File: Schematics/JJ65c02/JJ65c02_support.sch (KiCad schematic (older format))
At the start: 26 parts, among them SW1 RESET, U1 NE555, U2 74HC00, U3 74AC138, U4 74HC08, U5 MAX232B, U6 LM386, X1 1Mhz, X2 1.8Mhz

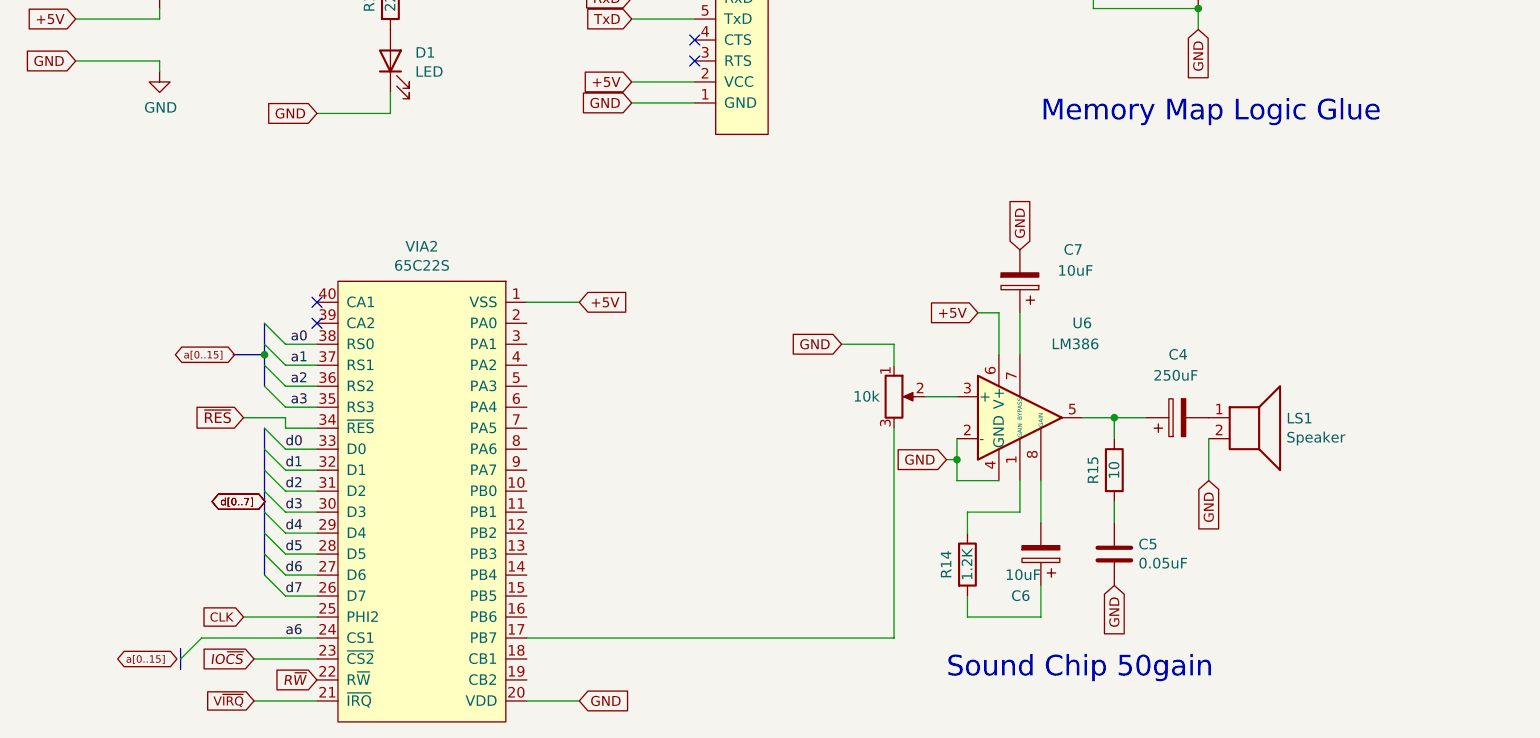
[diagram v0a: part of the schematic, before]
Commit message: Add in basic sound capability
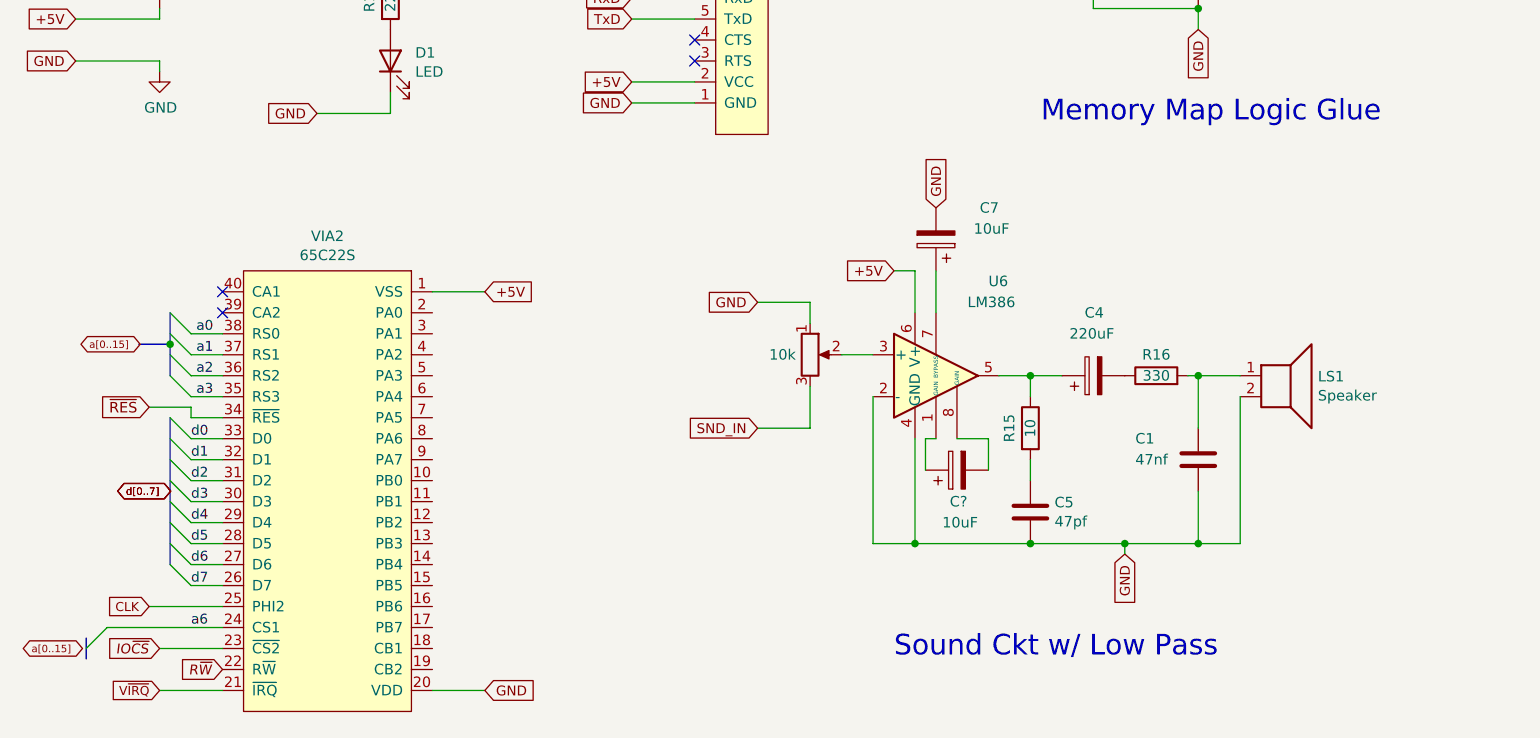
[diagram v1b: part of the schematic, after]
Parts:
- removed C6: 10uF, Capacitor_THT:C_Disc_D3.4mm_W2.1mm_P2.50mm, symbol Device:CP
- removed R14: 1.2K, Resistor_THT:R_Axial_DIN0207_L6.3mm_D2.5mm_P7.62mm_Horizontal, symbol Device:R
- added C1: 47nf, Capacitor_THT:C_Disc_D3.4mm_W2.1mm_P2.50mm, symbol Device:C
- added C?: 10uF, Capacitor_THT:C_Disc_D3.4mm_W2.1mm_P2.50mm, symbol Device:CP
- added R16: 330, Resistor_THT:R_Axial_DIN0207_L6.3mm_D2.5mm_P7.62mm_Horizontal, symbol Device:R
- C4: value 250uF -> 220uF
- C5: value 0.05uF -> 47pf
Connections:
- net GND: now also C1.2
- net at VIA2.17 (PB7): no longer RV2.3
- net at U6.1 (GAIN): now also C?.1
- net at U6.8 (GAIN): now also C?.2
- net at C4.2: now also R16.1; no longer LS1.1
- new net: C1.1, LS1.1, R16.2
- new net SND_IN: RV2.3
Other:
- note added: "Sound Ckt w/ Low Pass"
- note removed: "Sound Chip 50gain"
- moved on the sheet: C4, C5, C7, LS1, R15, U6, VIA2

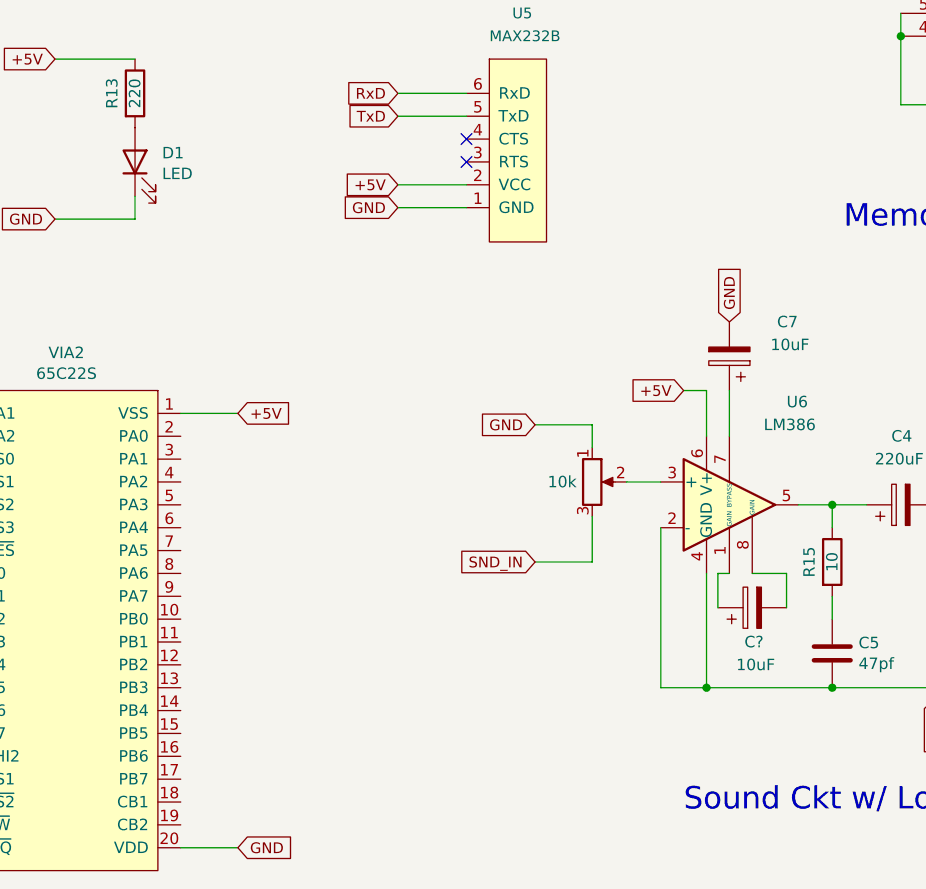
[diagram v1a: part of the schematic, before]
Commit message: Add the SND output to an LED indicator as well as the input to the amp
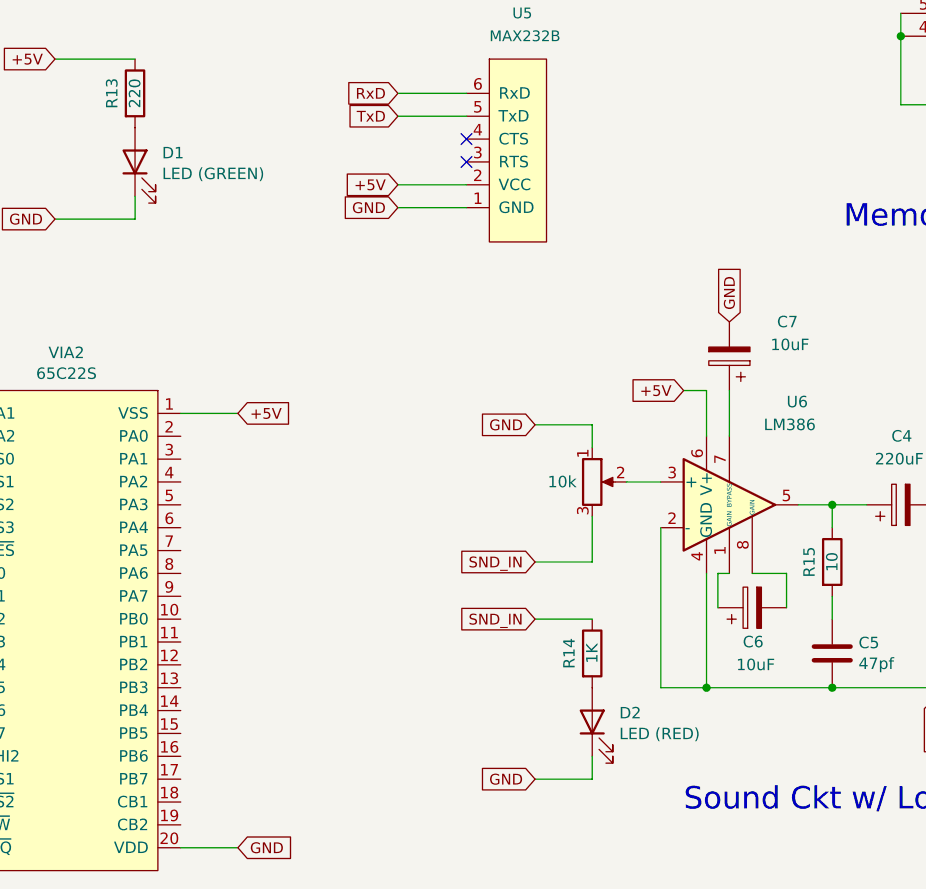
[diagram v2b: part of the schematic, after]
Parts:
- added D2: LED (RED), symbol Device:LED
- added R14: 1K, Resistor_THT:R_Axial_DIN0207_L6.3mm_D2.5mm_P7.62mm_Horizontal, symbol Device:R
- D1: value LED -> LED (GREEN)
- gave numbers to parts that had none: 1
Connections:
- net GND: now also D2.1 (K)
- net SND_IN: now also R14.1
- new net: D2.2 (A), R14.2
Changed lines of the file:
@@
 P 2450 3650
 F 0 "D1" V 2489 3532 50  0000 R CNN
-F 1 "LED" V 2398 3532 50  0000 R CNN
+F 1 "LED (GREEN)" V 2398 3532 50  0000 R CNN
 F 2 "" H 2450 3650 50  0001 C CNN
 F 3 "~" H 2450 3650 50  0001 C CNN
@@
 	4450 5400 4200 5400
 $Comp
-L Device:CP C?
+L Device:CP C6
 U 1 1 61A13E6D
 P 5150 5600
-AR Path="/61660CAC/61A13E6D" Ref="C?"  Part="1"
+AR Path="/61660CAC/61A13E6D" Ref="C6"  Part="1"
 AR Path="/61610474/61A13E6D" Ref="C?"  Part="1"
-F 0 "C?" V 5000 5550 50  0000 L CNN
+F 0 "C6" V 5000 5550 50  0000 L CNN
 F 1 "10uF" V 4900 5500 50  0000 L CNN
 F 2 "Capacitor_THT:C_Disc_D3.4mm_W2.1mm_P2.50mm" H 5188 5450 50  0001 C CNN
@@
 Wire Wire Line
 	5300 5450 5300 5600
+$Comp
+L Device:LED D2
+U 1 1 61AAFD1D
+P 4450 6100
+F 0 "D2" V 4489 5982 50  0000 R CNN
+F 1 "LED (RED)" V 4398 5982 50  0000 R CNN
+F 2 "" H 4450 6100 50  0001 C CNN
+F 3 "~" H 4450 6100 50  0001 C CNN
+	1    4450 6100
+	0    -1   -1   0
+$EndComp
+$Comp
+L Device:R R14
+U 1 1 61AAFD23
+P 4450 5800
+AR Path="/61660CAC/61AAFD23" Ref="R14"  Part="1"
+AR Path="/61610474/61AAFD23" Ref="R?"  Part="1"
+F 0 "R14" V 4350 5800 50  0000 C CNN
+F 1 "1K" V 4450 5800 50  0000 C CNN
+F 2 "Resistor_THT:R_Axial_DIN0207_L6.3mm_D2.5mm_P7.62mm_Horizontal" V 4380 5800 50  0001 C CNN
+F 3 "~" H 4450 5800 50  0001 C CNN
+	1    4450 5800
+	1    0    0    -1
+$EndComp
+Text GLabel 4200 5650 0    47   Input ~ 0
+SND_IN
+Text GLabel 4200 6350 0    47   Input ~ 0
+GND
+Wire Wire Line
+	4450 6350 4450 6250
+Wire Wire Line
+	4200 5650 4450 5650
+Wire Wire Line
+	4450 6350 4200 6350
 Wire Bus Line
 	1000 6400 1000 6500

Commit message: 2nd VIA
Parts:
- added A?: Arduino_Nano_v2.x, Module:Arduino_Nano, symbol MCU_Module:Arduino_Nano_v2.x
- added J?: Mini-DIN-6, symbol Connector:Mini-DIN-6
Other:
- moved on the sheet: X1, X2
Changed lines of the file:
@@
 L Oscillator:CXO_DIP14 X?
 U 1 1 6171CEB1
-P 8800 3650
+P 8700 3300
 AR Path="/6171CEB1" Ref="X?"  Part="1"
 AR Path="/61660CAC/6171CEB1" Ref="X1"  Part="1"
 AR Path="/61610474/6171CEB1" Ref="X?"  Part="1"
-F 0 "X1" H 8900 3900 50  0000 L CNN
-F 1 "1Mhz" H 8950 4000 50  0000 L CNN
-F 2 "Oscillator:Oscillator_DIP-14" H 9250 3300 50  0001 C CNN
-F 3 "http://cdn-reichelt.de/documents/datenblatt/B400/OSZI.pdf" H 8700 3650 50  0001 C CNN
-	1    8800 3650
-	1    0    0    -1
-$EndComp
-Text GLabel 9100 3650 2    43   Output ~ 0
+F 0 "X1" H 8800 3550 50  0000 L CNN
+F 1 "1Mhz" H 8850 3650 50  0000 L CNN
+F 2 "Oscillator:Oscillator_DIP-14" H 9150 2950 50  0001 C CNN
+F 3 "http://cdn-reichelt.de/documents/datenblatt/B400/OSZI.pdf" H 8600 3300 50  0001 C CNN
+	1    8700 3300
+	1    0    0    -1
+$EndComp
+Text GLabel 9000 3300 2    43   Output ~ 0
 CLK
 $Comp
 L power:+5V #PWR?
 U 1 1 6171CEBE
-P 8850 3700
+P 8750 3350
 AR Path="/6171CEBE" Ref="#PWR?"  Part="1"
 AR Path="/61660CAC/6171CEBE" Ref="#PWR020"  Part="1"
 AR Path="/61610474/6171CEBE" Ref="#PWR?"  Part="1"
-F 0 "#PWR020" H 8850 3550 50  0001 C CNN
-F 1 "+5V" H 8865 3873 50  0000 C CNN
-F 2 "" H 8850 3700 50  0001 C CNN
-F 3 "" H 8850 3700 50  0001 C CNN
-	1    8850 3700
-	1    0    0    -1
-$EndComp
-NoConn ~ 8500 3650
+F 0 "#PWR020" H 8750 3200 50  0001 C CNN
+F 1 "+5V" H 8765 3523 50  0000 C CNN
+F 2 "" H 8750 3350 50  0001 C CNN
+F 3 "" H 8750 3350 50  0001 C CNN
+	1    8750 3350
+	1    0    0    -1
+$EndComp
+NoConn ~ 8400 3300
 $Comp
 L Oscillator:CXO_DIP14 X?
 U 1 1 6171CEC5
-P 10150 3650
+P 10050 3300
 AR Path="/6171CEC5" Ref="X?"  Part="1"
 AR Path="/61660CAC/6171CEC5" Ref="X2"  Part="1"
 AR Path="/61610474/6171CEC5" Ref="X?"  Part="1"
-F 0 "X2" H 10250 3900 50  0000 L CNN
-F 1 "1.8Mhz" H 10300 4000 50  0000 L CNN
-F 2 "Oscillator:Oscillator_DIP-14" H 10600 3300 50  0001 C CNN
-F 3 "http://cdn-reichelt.de/documents/datenblatt/B400/OSZI.pdf" H 10050 3650 50  0001 C CNN
-	1    10150 3650
-	1    0    0    -1
-$EndComp
-Text GLabel 10450 3650 2    43   Output ~ 0
+F 0 "X2" H 10150 3550 50  0000 L CNN
+F 1 "1.8Mhz" H 10200 3650 50  0000 L CNN
+F 2 "Oscillator:Oscillator_DIP-14" H 10500 2950 50  0001 C CNN
+F 3 "http://cdn-reichelt.de/documents/datenblatt/B400/OSZI.pdf" H 9950 3300 50  0001 C CNN
+	1    10050 3300
+	1    0    0    -1
+$EndComp
+Text GLabel 10350 3300 2    43   Output ~ 0
 ACIA-CLK
-NoConn ~ 9850 3650
+NoConn ~ 9750 3300
 $Comp
 L 74xx:74HC00 U2
@@
 a12
 Wire Wire Line
-	8800 3300 8800 3350
+	8700 2950 8700 3000
 $Comp
 L 74xx:74LS138 U3
@@
 Text GLabel 1200 2400 0    47   Input ~ 0
 GND
-Text GLabel 10150 4000 3    47   Input ~ 0
+Text GLabel 10050 3650 3    47   Input ~ 0
 GND
 Text GLabel 6300 3500 3    47   Input ~ 0
@@
 Text GLabel 6700 2050 1    47   Input ~ 0
 +5V
-Text GLabel 8800 3300 1    47   Input ~ 0
-+5V
-Text GLabel 10150 3250 1    47   Input ~ 0
-+5V
-Text GLabel 8800 3950 3    47   Input ~ 0
-GND
-Wire Wire Line
-	10150 3250 10150 3350
-Wire Wire Line
-	10150 3950 10150 4000
+Text GLabel 8700 2950 1    47   Input ~ 0
++5V
+Text GLabel 10050 2900 1    47   Input ~ 0
++5V
+Text GLabel 8700 3600 3    47   Input ~ 0
+GND
+Wire Wire Line
+	10050 2900 10050 3000
+Wire Wire Line
+	10050 3600 10050 3650
 $Comp
 L 74xx:74LS08 U4
@@
 Wire Wire Line
 	4450 6350 4200 6350
+$Comp
+L MCU_Module:Arduino_Nano_v2.x A?
+U 1 1 61B02721
+P 7950 5150
+F 0 "A?" H 7950 4061 50  0000 C CNN
+F 1 "Arduino_Nano_v2.x" H 7950 3970 50  0000 C CNN
+F 2 "Module:Arduino_Nano" H 7950 5150 50  0001 C CIN
+F 3 "https://www.arduino.cc/en/uploads/Main/ArduinoNanoManual23.pdf" H 7950 5150 50  0001 C CNN
+	1    7950 5150
+	1    0    0    -1
+$EndComp
+$Comp
+L Connector:Mini-DIN-6 J?
+U 1 1 61B062BD
+P 9800 5200
+F 0 "J?" H 9800 5567 50  0000 C CNN
+F 1 "Mini-DIN-6" H 9800 5476 50  0000 C CNN
+F 2 "" H 9800 5200 50  0001 C CNN
+F 3 "http://service.powerdynamics.com/ec/Catalog17/Section%2011.pdf" H 9800 5200 50  0001 C CNN
+	1    9800 5200
+	1    0    0    -1
+$EndComp
 Wire Bus Line
 	1000 6400 1000 6500

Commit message: PCB work
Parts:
- removed D2: LED (RED), symbol Device:LED
- removed R14: 1K, Resistor_THT:R_Axial_DIN0207_L6.3mm_D2.5mm_P7.62mm_Horizontal, symbol Device:R
- removed R2: 4.7K, Resistor_THT:R_Axial_DIN0207_L6.3mm_D2.5mm_P7.62mm_Horizontal, symbol Device:R
- removed U4: 74HC08, Package_DIP:DIP-14_W7.62mm_Socket, symbol 74xx:74LS08
- added J2: Barrel_Jack, Connector_BarrelJack:CUI_PJ-059AH, symbol Connector:Barrel_Jack_Switch_Pin3Ring
- added J3: VIA2 PortB, Connector_PinSocket_2.54mm:PinSocket_1x10_P2.54mm_Vertical, symbol Connector_Generic:Conn_01x10
- added J4: Arduino Jack1, Connector_PinSocket_2.54mm:PinSocket_1x14_P2.54mm_Vertical, symbol Connector_Generic:Conn_01x14
- added J5: Arduino Jack2, Connector_PinSocket_2.54mm:PinSocket_1x14_P2.54mm_Vertical, symbol Connector_Generic:Conn_01x14
- added J6: AudioJack2, Connector_Audio:Jack_3.5mm_CUI_SJ1-3533NG_Horizontal, symbol Connector:AudioJack3
- added SW2: SW_SPST, Button_Switch_THT:SW_DIP_SPSTx01_Slide_6.7x4.1mm_W7.62mm_P2.54mm_LowProfile, symbol Switch:SW_SPST
- added unit 5 of U3
- added U7: LM2940T-5.0/LF08, Connector:LM2940, symbol Regulator_Linear:LM2936-5.0
- C3: renamed from C7; footprint Capacitor_THT:C_Disc_D3.4mm_W2.1mm_P2.50mm -> Capacitor_THT:CP_Radial_D5.0mm_P2.50mm
- C4: renamed from C6; footprint Capacitor_THT:C_Disc_D3.4mm_W2.1mm_P2.50mm -> Capacitor_THT:CP_Radial_D5.0mm_P2.50mm
- C6: renamed from C4; footprint Capacitor_THT:C_Disc_D3.4mm_W2.1mm_P2.50mm -> Capacitor_THT:CP_Radial_D6.3mm_P2.50mm
- D1: footprint (none) -> LED_THT:LED_D3.0mm_FlatTop
- J1: renamed from J?; footprint (none) -> JJ65c02:mini_din-6
- LS1: footprint (none) -> JJ65c02:MiniSpeaker
- SW1: footprint Button_Switch_THT:SW_PUSH_6mm_H4.3mm -> Button_Switch_THT:SW_PUSH_6mm
- U2: renamed from U1; symbol JJ65c02-rescue:NE555-Timer-6502 -> Timer:LM555xN
- U4: renamed from U5; footprint TerminalBlock_TE-Connectivity:TerminalBlock_TE_282834-6_1x06_P2.54mm_Horizontal -> JJ65c02:maxboard
- U6: footprint (none) -> Package_DIP:DIP-8_W7.62mm_Socket
- gave numbers to parts that had none: 1
- renumbered C2 to C1, C3 to C2, C1 to C7, R7 to R11, R13 to R12, R8 to R13, R9 to R14, U2 to U3, U3 to U5
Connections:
- net +5V: now also A1.30 (VIN), J1.4, VIA2.20 (VDD), J5.12 (Pin_12), U3.14 (VCC), U7.3 (VO); no longer VIA2.1 (VSS)
- net GND: now also A1.29 (GND), A1.4 (GND), J1.3, VIA2.1 (VSS), J2.2, J2.3, J5.13 (Pin_13), J6.S, U3.7 (GND), U7.2 (GND); no longer VIA2.20 (VDD)
- net at VIA2.10 (PB0): now also J3.1 (Pin_1)
- net at VIA2.11 (PB1): now also J3.2 (Pin_2)
- net at VIA2.12 (PB2): now also J3.3 (Pin_3)
- net at VIA2.13 (PB3): now also J3.4 (Pin_4)
- net at VIA2.14 (PB4): now also J3.5 (Pin_5)
- net at VIA2.15 (PB5): now also J3.6 (Pin_6)
- net at VIA2.16 (PB6): now also J3.7 (Pin_7)
- net at VIA2.17 (PB7): now also J3.8 (Pin_8)
- net at VIA2.18 (CB1): now also J3.9 (Pin_9)
- net at VIA2.19 (CB2): now also J3.10 (Pin_10)
- net nd6: now reaches VIA2.2 (PA0)
- net nd6: now also A1.9 (D6), J4.7 (Pin_7)
- net nd7: now reaches VIA2.3 (PA1)
- net nd7: now also A1.10 (D7), J4.8 (Pin_8)
- net nd8: now reaches VIA2.4 (PA2)
- net nd8: now also A1.11 (D8), J4.9 (Pin_9)
- net nd5: now reaches VIA2.40 (CA1)
- net nd5: now also A1.8 (D5), J4.6 (Pin_6)
- net nd9: now reaches VIA2.5 (PA3)
- net nd9: now also A1.12 (D9), J4.10 (Pin_10)
- net nd10: now reaches VIA2.6 (PA4)
- net nd10: now also A1.13 (D10), J4.11 (Pin_11)
- net nd11: now reaches VIA2.7 (PA5)
- net nd11: now also A1.14 (D11), J4.12 (Pin_12)
- net nd12: now reaches VIA2.8 (PA6)
- net nd12: now also A1.15 (D12), J4.13 (Pin_13)
- net nd13: now reaches VIA2.9 (PA7)
- net nd13: now also A1.16 (D13), J4.14 (Pin_14)
- net at C7.1, R16.2: now also J6.R, J6.T, SW2.1 (A); no longer LS1.1
- net nd1: now reaches A1.1 (D1/TX)
- net nd1: now also J4.2 (Pin_2)
- net ndrf: now reaches A1.18 (AREF)
- net ndrf: now also J5.9 (Pin_9)
- net na0: now reaches A1.19 (A0)
- net na0: now also J5.8 (Pin_8)
- net nd0: now reaches A1.2 (D0/RX)
- net nd0: now also J4.1 (Pin_1)
- net na1: now reaches A1.20 (A1)
- net na1: now also J5.7 (Pin_7)
- net na2: now reaches A1.21 (A2)
- net na2: now also J5.6 (Pin_6)
- net na3: now reaches A1.22 (A3)
- net na3: now also J5.5 (Pin_5)
- net na4: now reaches A1.23 (A4)
- net na4: now also J5.4 (Pin_4)
- net na5: now reaches A1.24 (A5)
- net na5: now also J5.3 (Pin_3)
- net na6: now reaches A1.25 (A6)
- net na6: now also J5.2 (Pin_2)
- net na7: now reaches A1.26 (A7)
- net na7: now also J5.1 (Pin_1)
- net ndr2: now reaches A1.28 (~RESET)
- net ndr2: now also J5.11 (Pin_11)
- net ndr1: now reaches A1.3 (~RESET)
- net ndr1: now also J5.10 (Pin_10)
- net nd2: now reaches A1.5 (D2)
- net nd2: now also J1.5, J4.3 (Pin_3)
- net nd3: now reaches A1.6 (D3)
- net nd3: now also J4.4 (Pin_4)
- net nd4: now reaches A1.7 (D4)
- net nd4: now also J1.1, J4.5 (Pin_5)
- net V~IRQ renamed V2~IRQ
- new net: J2.1, U7.1 (VI)
- new net: LS1.1, SW2.2 (B)
- no-connect marks 14 -> 18
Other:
- note removed: "~IRQ~ Logic Glue"
- moved on the sheet: A1, C3, C4, C5, C6, C7, D1, J1, LS1, R12, R15, R16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
